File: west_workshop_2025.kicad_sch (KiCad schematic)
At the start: 4 parts

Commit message: Schematic Done - Ready for layout
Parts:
- added A1: RaspberryPi_Pico, 0_west_footprints:RaspberryPi_Pico, symbol 0_west_symbols:RaspberryPi_Pico
- added D1, D2, D3, D4, D5, D6, D7, D8, D9: LED, 0_west_footprints:Kingbright_WP914x, symbol 0_west_symbols:LED
- added D10, D11, D12, D13, D14, D15, D16, D17, D18: 1N4148, Diode_THT:D_DO-35_SOD27_P7.62mm_Horizontal, symbol 0_west_symbols:DIODE
- added Q1: TN0604, Package_TO_SOT_THT:TO-92L_Inline, symbol 0_west_symbols:NMOS
- added R1, R10, R2, R3, R4, R5, R6, R7, R8, R9: 390R, Resistor_THT:R_Axial_DIN0204_L3.6mm_D1.6mm_P5.08mm_Horizontal, symbol 0_west_symbols:Resistor
- added R11: 10k, Resistor_THT:R_Axial_DIN0204_L3.6mm_D1.6mm_P5.08mm_Horizontal, symbol 0_west_symbols:Resistor
- added SW1, SW2, SW3, SW4, SW5, SW6, SW7, SW8, SW9: switch_1.00u, 0_west_footprints:SW_Cherry_MX_PCB_1.00u, symbol 0_west_symbols:Switch_Push
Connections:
- new net: D1.1 (K), D2.1 (K), D3.1 (K), D4.1 (K), D5.1 (K), D6.1 (K), D7.1 (K), D8.1 (K), D9.1 (K), Q1.1 (D)
- new net: D1.2 (A), R1.2
- new net: D16.1 (K), SW7.1
- new net: D6.2 (A), R6.2
- new net: D4.2 (A), R4.2
- new net: D17.1 (K), SW8.1
- new net: D15.1 (K), SW6.1
- new net: D9.2 (A), R9.2
- new net: D2.2 (A), R2.2
- new net: D10.1 (K), SW1.1
- new net: D5.2 (A), R5.2
- new net: D14.1 (K), SW5.1
- new net: D13.1 (K), SW4.1
- new net: D3.2 (A), R3.2
- new net: D11.1 (K), SW2.1
- new net: D18.1 (K), SW9.1
- new net: D12.1 (K), SW3.1
- new net: D7.2 (A), R7.2
- new net: D8.2 (A), R8.2
- new net +3V3: A1.36 (3V3)
- new net +5V: A1.39 (VSYS), A1.40 (VBUS), R1.1, R2.1, R3.1, R4.1, R5.1, R6.1, R7.1, R8.1, R9.1
- new net GND: A1.13 (GND), A1.18 (GND), A1.23 (GND), A1.28 (GND), A1.3 (GND), A1.33 (AGND), A1.38 (GND), A1.8 (GND), Q1.3 (S), R11.2
- new net collumn_1: A1.1 (GPIO0), SW1.2, SW4.2, SW7.2
- new net collumn_2: A1.2 (GPIO1), SW2.2, SW5.2, SW8.2
- new net collumn_3: A1.4 (GPIO2), SW3.2, SW6.2, SW9.2
- new net fet_gate: Q1.2 (G), R10.2, R11.1
- new net led_ctrl: A1.9 (GPIO6), R10.1
- new net row_1: A1.5 (GPIO3), D10.2 (A), D11.2 (A), D12.2 (A)
- new net row_2: A1.6 (GPIO4), D13.2 (A), D14.2 (A), D15.2 (A)
- new net row_3: A1.7 (GPIO5), D16.2 (A), D17.2 (A), D18.2 (A)
- no-connect marks 0 -> 22
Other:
- note added: "3V3 DRIVEN"
- note added: "INTERNAL PU RESISTORS SW DEBOUNCING"
- note added: "TOTAL 9x8mA=72mA"
- note added: "Vdrop ~1.9V Idesired ~8mA Rlimit = (5-1.9)/8mA = 387.5Ω"
- note removed: "-- Blank Schematic --"

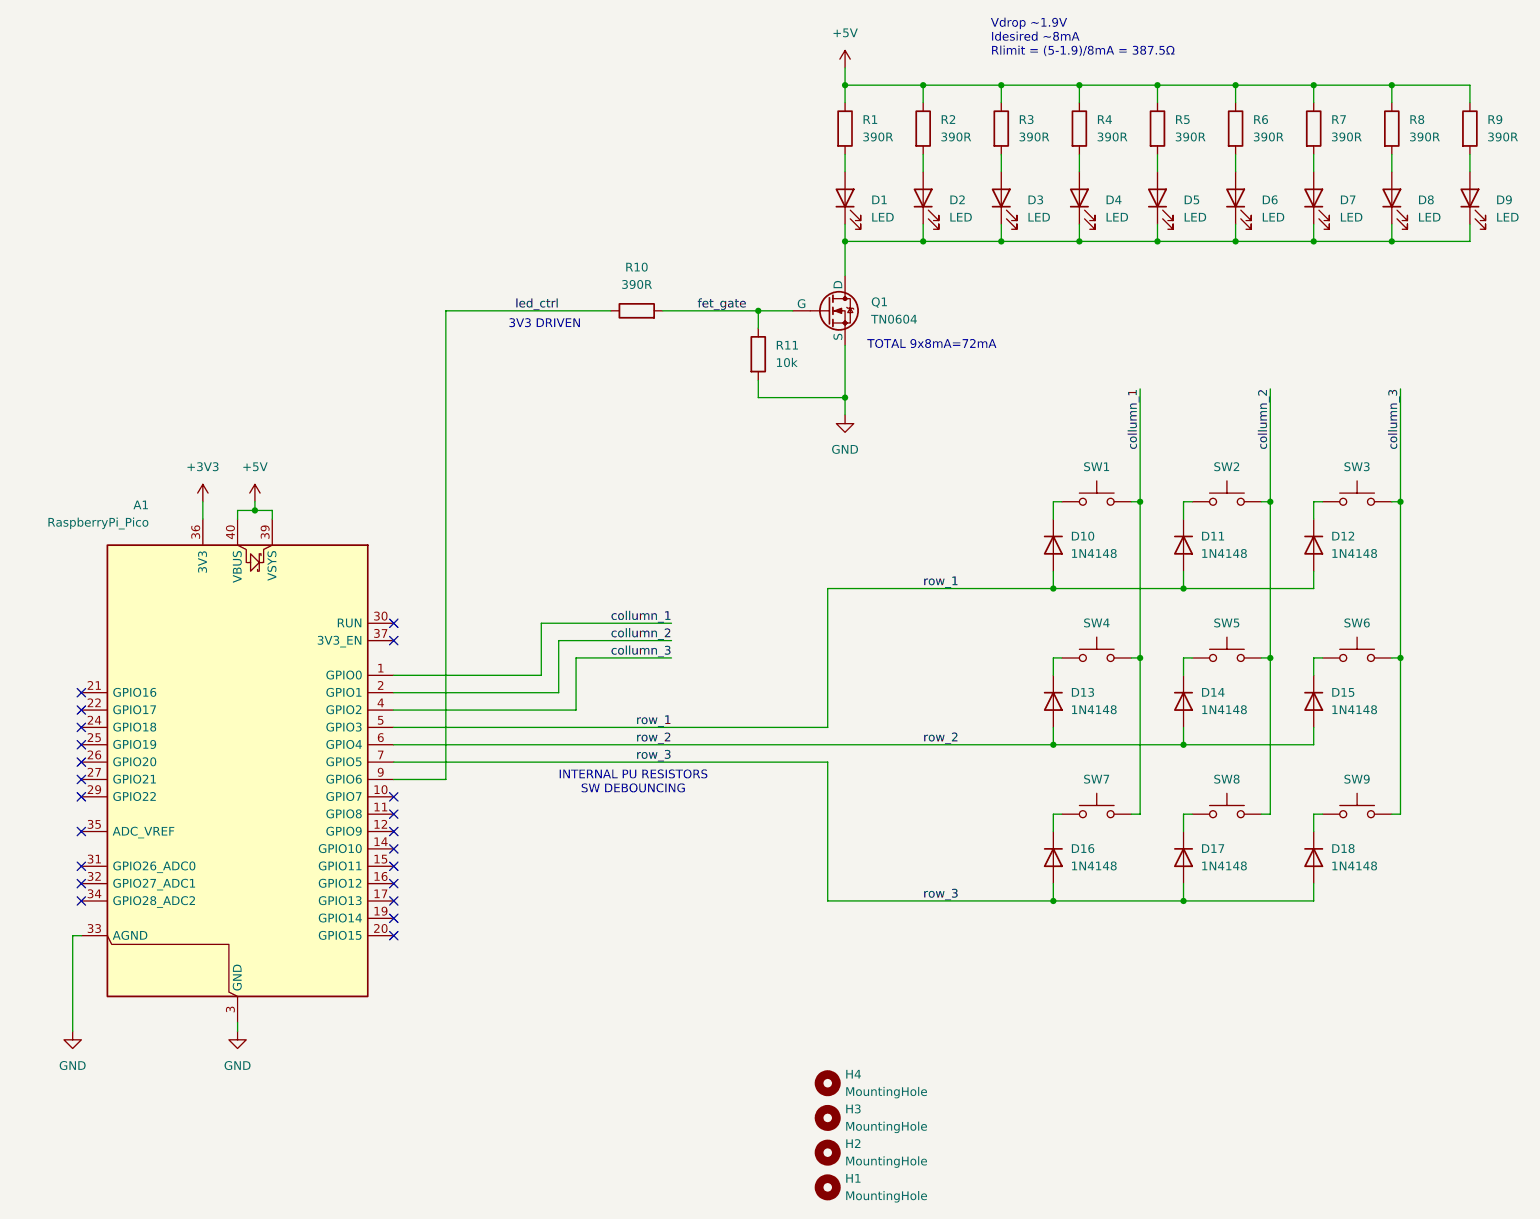
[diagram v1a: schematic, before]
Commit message: Revert Change - Release issues
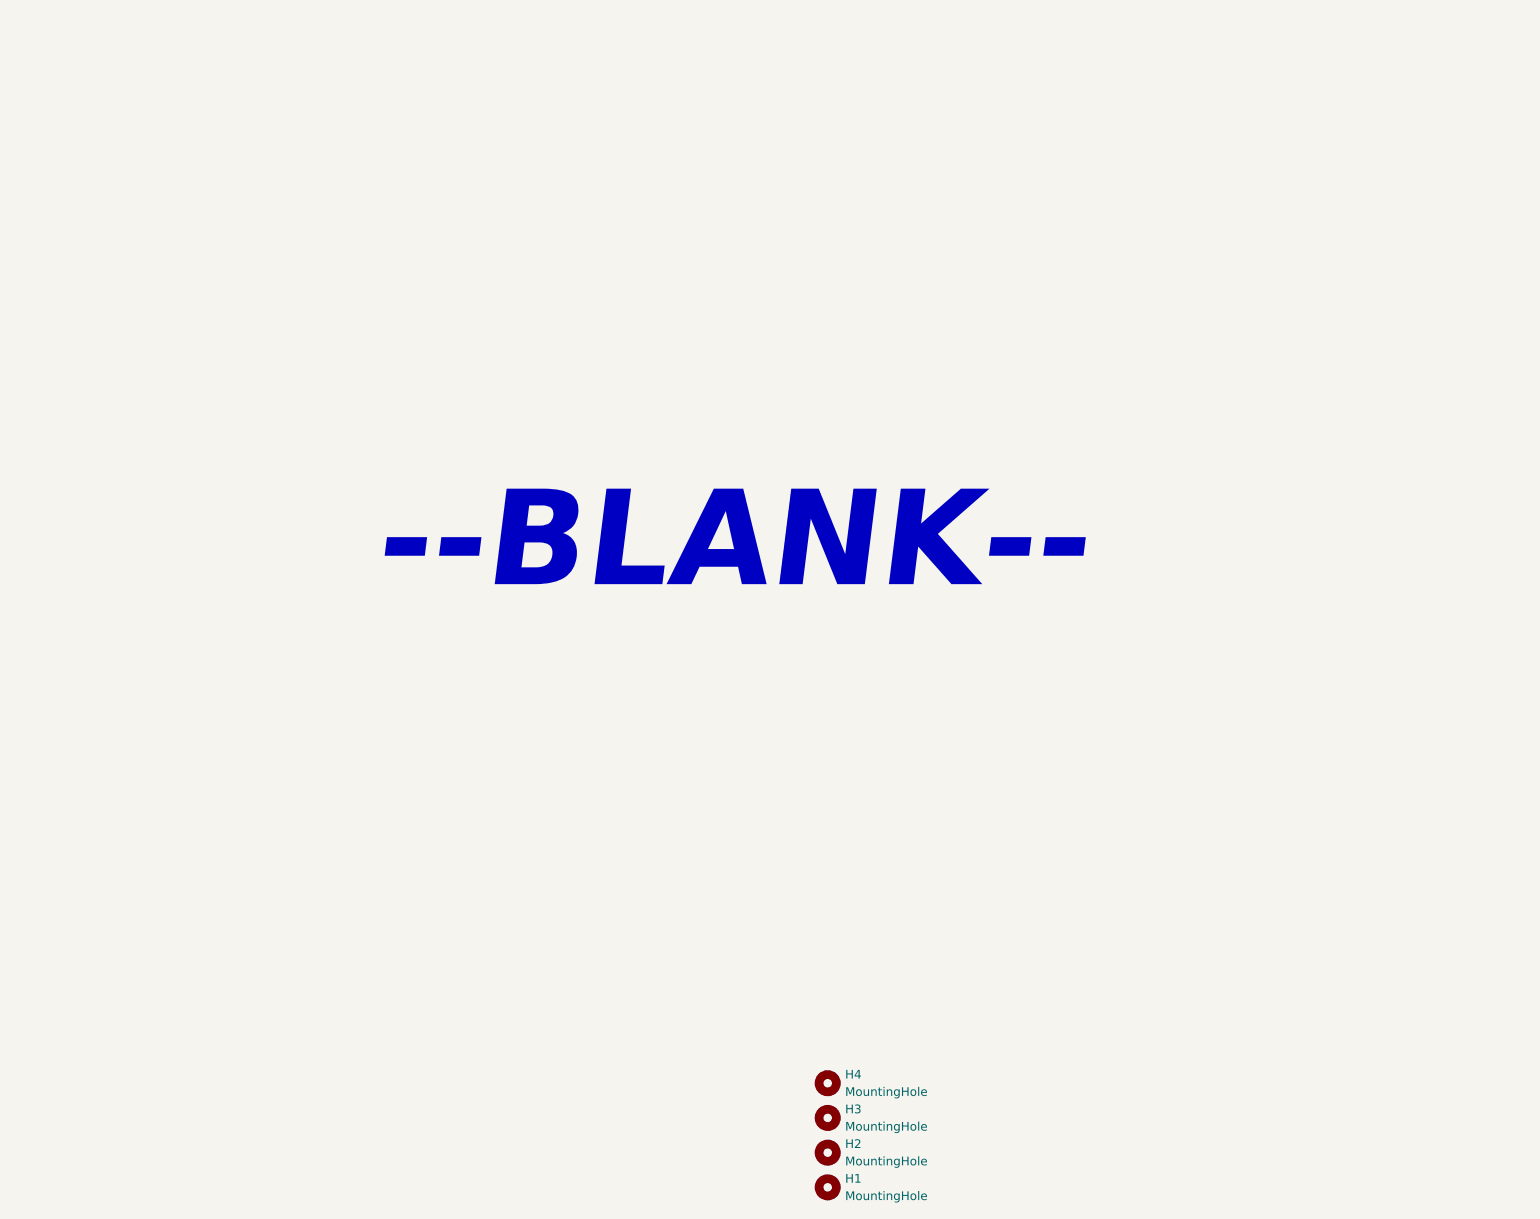
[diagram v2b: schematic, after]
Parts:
- removed A1: RaspberryPi_Pico, 0_west_footprints:RaspberryPi_Pico, symbol 0_west_symbols:RaspberryPi_Pico
- removed D1, D2, D3, D4, D5, D6, D7, D8, D9: LED, 0_west_footprints:Kingbright_WP914x, symbol 0_west_symbols:LED
- removed D10, D11, D12, D13, D14, D15, D16, D17, D18: 1N4148, Diode_THT:D_DO-35_SOD27_P7.62mm_Horizontal, symbol 0_west_symbols:DIODE
- removed Q1: TN0604, Package_TO_SOT_THT:TO-92L_Inline, symbol 0_west_symbols:NMOS
- removed R1, R10, R2, R3, R4, R5, R6, R7, R8, R9: 390R, Resistor_THT:R_Axial_DIN0204_L3.6mm_D1.6mm_P5.08mm_Horizontal, symbol 0_west_symbols:Resistor
- removed R11: 10k, Resistor_THT:R_Axial_DIN0204_L3.6mm_D1.6mm_P5.08mm_Horizontal, symbol 0_west_symbols:Resistor
- removed SW1, SW2, SW3, SW4, SW5, SW6, SW7, SW8, SW9: switch_1.00u, 0_west_footprints:SW_Cherry_MX_PCB_1.00u, symbol 0_west_symbols:Switch_Push
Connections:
- no-connect marks 22 -> 0
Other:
- note added: "--BLANK--"
- note removed: "3V3 DRIVEN"
- note removed: "INTERNAL PU RESISTORS SW DEBOUNCING"
- note removed: "TOTAL 9x8mA=72mA"
- note removed: "Vdrop ~1.9V Idesired ~8mA Rlimit = (5-1.9)/8mA = 387.5Ω"
